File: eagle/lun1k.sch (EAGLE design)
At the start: 102 parts, among them IC1 MCP1700, IC2 LM27313, IC3 STM32F405RGT, IC4 NRF24L01SMD, IC5 MCP73833, J2 XF2-3015-1LW, Q1 Q12M-SMD-S, Q2 3.2X2.5CRYSTAL, SW1 JS102011SAQN, T1 SI2301DS, T5 SI2301DS, T6 SI2301DS, U1 N35P112, X1 MICROUSB, X1_ JST-PH3

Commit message: placed buttons
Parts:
- added SW2, SW3, SW4: SWITCH_MCTAEF, seb:SWITCH_MCTAEF
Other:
- note added: "BUTTONS"
- note added: "JOYSTICK"
- note removed: "NAVIGATION BUTTON"
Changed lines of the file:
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@@
 <layer number="110" name="fp0" color="7" fill="1" visible="no" active="yes"/>
 <layer number="111" name="LPC17xx" color="7" fill="1" visible="yes" active="yes"/>
+<layer number="112" name="tSilk" color="7" fill="1" visible="yes" active="yes"/>
 <layer number="116" name="Patch_BOT" color="9" fill="4" visible="yes" active="yes"/>
 <layer number="121" name="_tsilk" color="7" fill="1" visible="yes" active="yes"/>
@@
 <layer number="124" name="bTestmark" color="7" fill="1" visible="no" active="yes"/>
 <layer number="125" name="_tNames" color="7" fill="1" visible="yes" active="yes"/>
+<layer number="126" name="_bNames" color="7" fill="1" visible="yes" active="yes"/>
+<layer number="127" name="_tValues" color="7" fill="1" visible="yes" active="yes"/>
+<layer number="128" name="_bValues" color="7" fill="1" visible="yes" active="yes"/>
 <layer number="131" name="tAdjust" color="7" fill="1" visible="no" active="yes"/>
 <layer number="132" name="bAdjust" color="7" fill="1" visible="no" active="yes"/>
 <layer number="144" name="Drill_legend" color="7" fill="1" visible="yes" active="yes"/>
 <layer number="151" name="HeatSink" color="7" fill="1" visible="yes" active="yes"/>
+<layer number="152" name="_bDocu" color="7" fill="1" visible="yes" active="yes"/>
 <layer number="199" name="Contour" color="7" fill="1" visible="yes" active="yes"/>
 <layer number="200" name="200bmp" color="1" fill="10" visible="yes" active="yes"/>
@@
 <layer number="223" name="223bmp" color="24" fill="1" visible="no" active="no"/>
 <layer number="224" name="224bmp" color="25" fill="1" visible="no" active="no"/>
+<layer number="248" name="Housing" color="7" fill="1" visible="yes" active="yes"/>
+<layer number="249" name="Edge" color="7" fill="1" visible="yes" active="yes"/>
 <layer number="250" name="Descript" color="3" fill="1" visible="no" active="no"/>
 <layer number="251" name="SMDround" color="12" fill="11" visible="no" active="no"/>
@@
 <part name="R28" library="SparkFun" deviceset="RESISTOR" device="0402-RES" value="10k"/>
 <part name="R29" library="SparkFun" deviceset="RESISTOR" device="0402-RES" value="10k"/>
+<part name="SW2" library="seb" deviceset="SWITCH_MCTAEF" device=""/>
+<part name="SW3" library="seb" deviceset="SWITCH_MCTAEF" device=""/>
+<part name="SW4" library="seb" deviceset="SWITCH_MCTAEF" device=""/>
 </parts>
 <sheets>
@@
 <text x="137.16" y="157.48" size="2.54" layer="94">LEDs</text>
 <text x="193.04" y="157.48" size="2.54" layer="94">(optional) SD CARD</text>
-<text x="345.44" y="157.48" size="2.54" layer="94">NAVIGATION BUTTON</text>
+<text x="345.44" y="157.48" size="2.54" layer="94">JOYSTICK</text>
 <text x="2.54" y="99.06" size="2.54" layer="94">CPU</text>
 <text x="180.34" y="114.3" size="2.54" layer="94">RADIO</text>
@@
 <text x="431.8" y="132.08" size="1.778" layer="91">Leave SJ1 open for I2C Addr 0x41</text>
 <text x="431.8" y="129.54" size="1.778" layer="91">Close SJ1 for I2C Addr 0x40</text>
+<text x="139.7" y="203.2" size="2.54" layer="94">BUTTONS</text>
 </plain>
 <instances>
@@
 <instance part="R28" gate="G$1" x="485.14" y="167.64" rot="R90"/>
 <instance part="R29" gate="G$1" x="495.3" y="167.64" rot="R90"/>
+<instance part="SW2" gate="G$1" x="157.48" y="172.72" smashed="yes" rot="MR0">
+<attribute name="NAME" x="149.225" y="168.91" size="1.778" layer="95" rot="MR0"/>
+</instance>
+<instance part="SW3" gate="G$1" x="157.48" y="180.34" smashed="yes" rot="MR0">
+<attribute name="NAME" x="149.225" y="176.53" size="1.778" layer="95" rot="MR0"/>
+</instance>
+<instance part="SW4" gate="G$1" x="157.48" y="187.96" smashed="yes" rot="MR0">
+<attribute name="NAME" x="149.225" y="184.15" size="1.778" layer="95" rot="MR0"/>
+</instance>
 </instances>
 <busses>

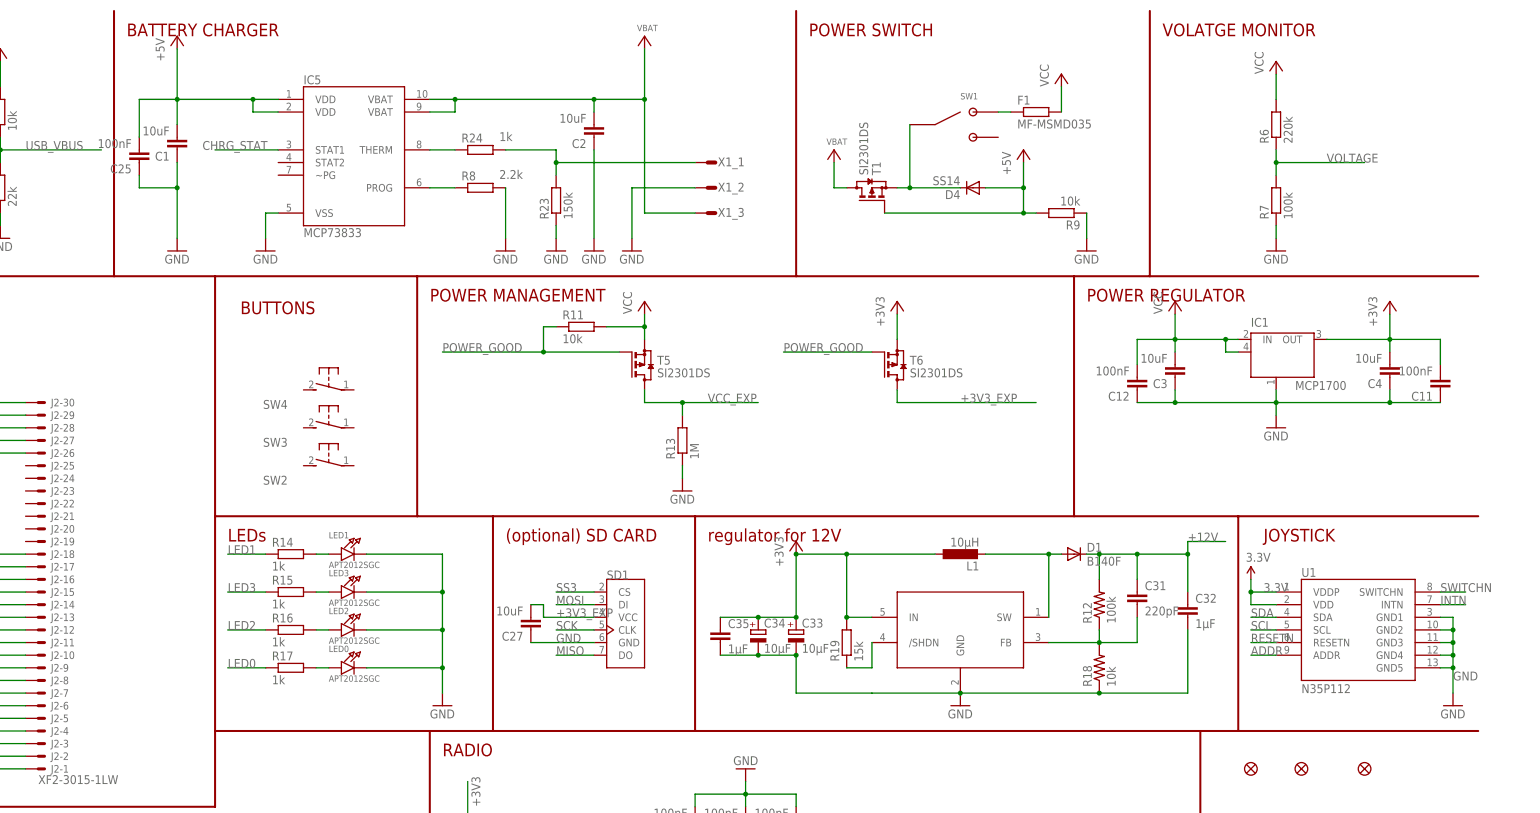
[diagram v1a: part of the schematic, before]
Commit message: completely removed old supply & management
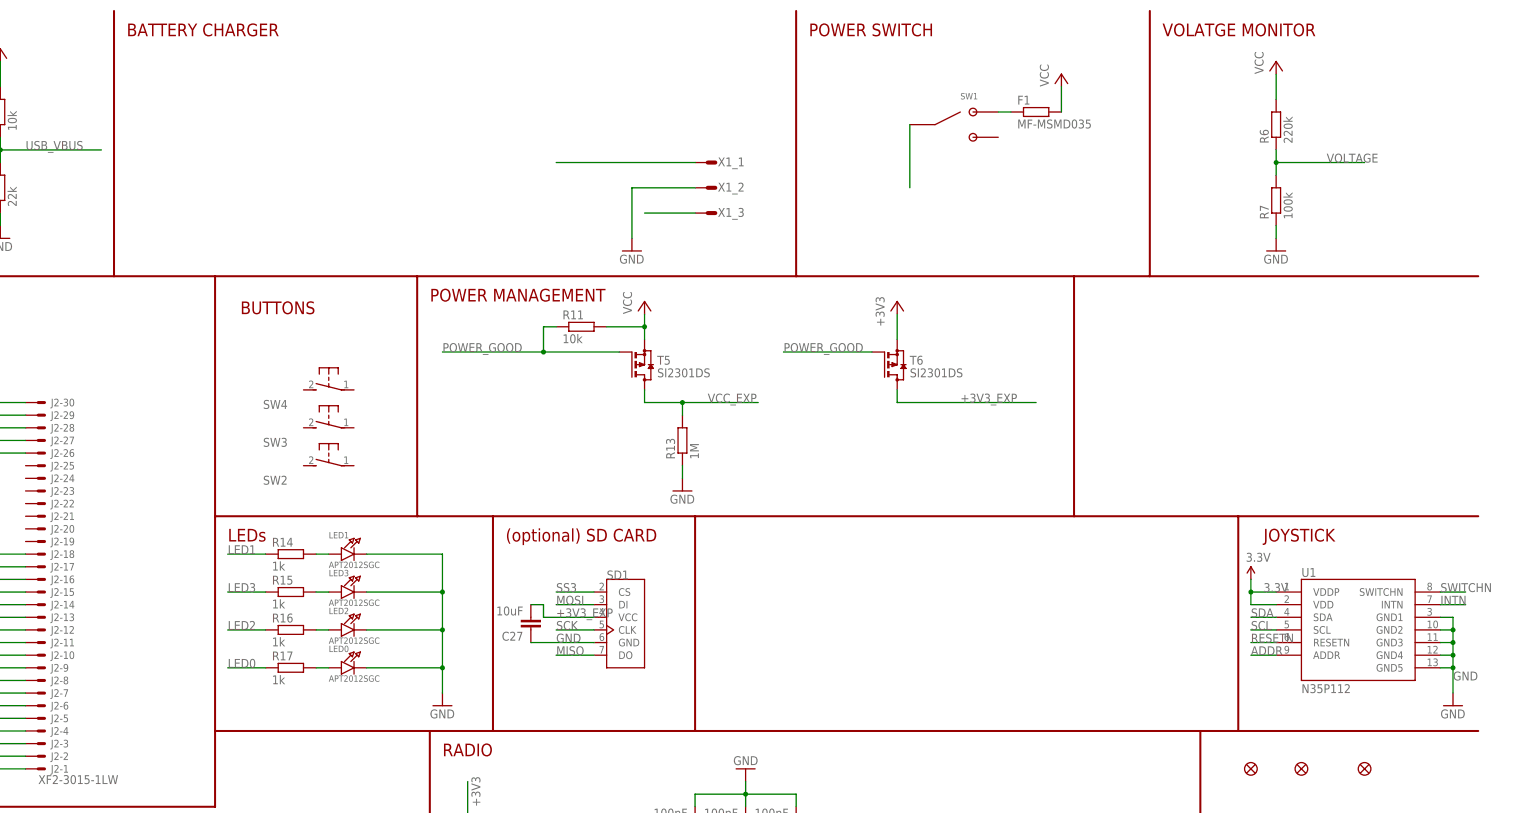
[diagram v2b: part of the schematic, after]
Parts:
- removed C1, C2, C3, C4: 10uF, rcl:C-EUC0805K
- removed C11, C12, C25: 100nF, SparkFun-Capacitors:CAP0402-CAP
- removed C31: 220pF, SparkFun:CAP0805
- removed C32, C35: 1µF, SparkFun:CAP0805
- removed C33, C34: 10µF, rcl:CPOL-EUSMCA
- removed D1: B140F, diode:DIODE-DO214AC
- removed D4: SS14, diode:DIODE-SMB
- removed IC1: MCP1700, badge:MCP1700
- removed IC2: LM27313, seb:LM27313
- removed IC5: MCP73833, SparkFun:MCP73833
- removed L1: 10µH, resistor:L-EUL1812
- removed R12: 100k, SparkFun:RESISTOR0805-RES
- removed R18: 10k, SparkFun:RESISTOR0805-RES
- removed R19: 15k, rcl:R-EU_R0402
- removed R23: 150k, rcl:R-EU_R0603
- removed R24: 1k, rcl:R-EU_R0603
- removed R8: 2.2k, rcl:R-EU_R0603
- removed R9: 10k, rcl:R-EU_R0603
- removed T1: SI2301DS, transistor-small-signal:BSS84
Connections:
- removed net CHRG_STAT: IC5.STAT1
- removed net N$13: IC5.PROG, R8.2
- removed net N$16: D1.A, IC2.SW, L1.2
- removed net N$17: C31.2, IC2.FB, R12.1, R18.2
- removed net N$18: IC2./SHDN, R19.1
- removed net N$2: IC5.THERM, R24.2
- removed net N$7: R23.2, R24.1, X1_1.1
- removed net VBAT: C2.2, IC5.VBAT@1, IC5.VBAT@2, T1.D, X1_3.1
- new net N$21: X1_3.1
- new net VLIPO: X1_1.1
- net +12V: no longer C31.1, C32.1, D1.C, R12.2
- net +3V3: no longer C11.2, C33.+, C34.+, C35.1, C4.2, IC1.OUT, IC2.IN, L1.1, R19.2
- net +5V: no longer C1.2, C25.2, D4.A, IC5.VDD@1, IC5.VDD@2, R9.2, T1.G
- net GND: no longer C1.1, C11.1, C12.1, C2.1, C25.1, C3.1, C32.2, C33.-, C34.-, C35.2, C4.1, IC1.GND/ADJ, IC2.GND, IC5.VSS, R18.1, R23.1, R8.1, R9.1
- net N$8: no longer D4.C, T1.S
- net VCC: no longer C12.2, C3.2, IC1.IN, IC1.IN@1
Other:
- note removed: "POWER REGULATOR"
- note removed: "regulator for 12V"

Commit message: some resistors: 0603 -> 0402
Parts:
- R11, R13, R2, R3, R4, R5, R6, R7: device rcl:R-EU_R0603 -> SparkFun-Passives:RESISTOR0402-RES
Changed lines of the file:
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@@
 <part name="P+5" library="supply1" deviceset="+5V" device=""/>
 <part name="GND9" library="supply1" deviceset="GND" device=""/>
-<part name="R4" library="rcl" deviceset="R-EU_" device="R0603" value="10k"/>
-<part name="R5" library="rcl" deviceset="R-EU_" device="R0603" value="22k"/>
+<part name="R4" library="SparkFun-Passives" deviceset="RESISTOR" device="0402-RES" value="10k"/>
+<part name="R5" library="SparkFun-Passives" deviceset="RESISTOR" device="0402-RES" value="22k"/>
 <part name="GND10" library="supply1" deviceset="GND" device=""/>
 <part name="P+6" library="supply1" deviceset="+5V" device=""/>
-<part name="R2" library="rcl" deviceset="R-EU_" device="R0603" value="33"/>
-<part name="R3" library="rcl" deviceset="R-EU_" device="R0603" value="33"/>
+<part name="R2" library="SparkFun-Passives" deviceset="RESISTOR" device="0402-RES" value="33"/>
+<part name="R3" library="SparkFun-Passives" deviceset="RESISTOR" device="0402-RES" value="33"/>
 <part name="GND11" library="supply1" deviceset="GND" device=""/>
 <part name="Q1" library="seb" deviceset="X22-OSCILLATOR" device="" value="Q12M-SMD-S"/>
@@
 <part name="+3V6" library="supply1" deviceset="+3V3" device=""/>
 <part name="P+10" library="supply1" deviceset="VCC" device=""/>
-<part name="R11" library="rcl" deviceset="R-EU_" device="R0603" value="10k"/>
-<part name="R6" library="rcl" deviceset="R-EU_" device="R0603" value="220k"/>
-<part name="R7" library="rcl" deviceset="R-EU_" device="R0603" value="100k"/>
+<part name="R11" library="SparkFun-Passives" deviceset="RESISTOR" device="0402-RES" value="10k"/>
+<part name="R6" library="SparkFun-Passives" deviceset="RESISTOR" device="0402-RES" value="220k"/>
+<part name="R7" library="SparkFun-Passives" deviceset="RESISTOR" device="0402-RES" value="100k"/>
 <part name="GND18" library="supply1" deviceset="GND" device=""/>
 <part name="P+7" library="supply1" deviceset="VCC" device=""/>
@@
 <part name="GND28" library="supply1" deviceset="GND" device=""/>
 <part name="R22" library="rcl" deviceset="R-EU_" device="R0603" value="R1002-1%63"/>
-<part name="R13" library="rcl" deviceset="R-EU_" device="R0603" value="1M"/>
+<part name="R13" library="SparkFun-Passives" deviceset="RESISTOR" device="0402-RES" value="1M"/>
 <part name="GND1" library="supply1" deviceset="GND" device=""/>
 <part name="X1_" library="badge" deviceset="JST-PH3" device=""/>

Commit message: some resistors: 0603 -> 0402
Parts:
- R14, R15, R16, R17: device rcl:R-EU_R0603 -> SparkFun-Passives:RESISTOR0402-RES
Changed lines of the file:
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@@
 <part name="LED2" library="microbuilder" deviceset="LED" device="0805" value="APT2012SGC"/>
 <part name="LED0" library="microbuilder" deviceset="LED" device="0805" value="APT2012SGC"/>
-<part name="R14" library="rcl" deviceset="R-EU_" device="R0603" value="1k"/>
+<part name="R14" library="SparkFun-Passives" deviceset="RESISTOR" device="0402-RES" value="1k"/>
 <part name="C9" library="SparkFun-Capacitors" deviceset="CAP" device="0402-CAP" value="22pF"/>
 <part name="P+5" library="supply1" deviceset="+5V" device=""/>
@@
 <part name="C10" library="SparkFun-Capacitors" deviceset="CAP" device="0402-CAP" value="22pF"/>
 <part name="GND13" library="supply1" deviceset="GND" device=""/>
-<part name="R15" library="rcl" deviceset="R-EU_" device="R0603" value="1k"/>
-<part name="R16" library="rcl" deviceset="R-EU_" device="R0603" value="1k"/>
-<part name="R17" library="rcl" deviceset="R-EU_" device="R0603" value="1k"/>
+<part name="R15" library="SparkFun-Passives" deviceset="RESISTOR" device="0402-RES" value="1k"/>
+<part name="R16" library="SparkFun-Passives" deviceset="RESISTOR" device="0402-RES" value="1k"/>
+<part name="R17" library="SparkFun-Passives" deviceset="RESISTOR" device="0402-RES" value="1k"/>
 <part name="+3V6" library="supply1" deviceset="+3V3" device=""/>
 <part name="P+10" library="supply1" deviceset="VCC" device=""/>

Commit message: new lipo charger
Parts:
- added C1, C12: 10µF, SparkFun:CAP0805
- added C11, C7: 10pF, SparkFun:CAP0805
- added C2: 22µF, SparkFun:CAP0805
- added C3: 33pF, SparkFun:CAP0805
- added C4: 330pF, SparkFun:CAP0805
- added C8: 1µF, SparkFun:CAP0805
- added IC1: LTC3558, seb:LTC3558
- added L1: 2,2µH, seb:SMD-INDUCTOR-4012
- added L5: 4,7µF, seb:VLF4012A
- added R12: 15k, SparkFun-Resistors:RESISTOR0805-RES
- added R18: 121k, SparkFun-Resistors:RESISTOR0805-RES
- added R19: 1k, SparkFun-Resistors:RESISTOR0805-RES
- added R24, R30, R31: 680k, SparkFun-Resistors:RESISTOR0402-RES
- added R32: 470k, SparkFun-Resistors:RESISTOR0805-RES
- added R33: 150k, SparkFun-Resistors:RESISTOR0805-RES
- added R8: 130k, SparkFun-Resistors:RESISTOR0805-RES
- added R9: 680k, SparkFun-Resistors:RESISTOR0805-RES
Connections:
- removed net N$15: F1.1, SW1.1
- removed net N$8: SW1.2
- new net EN2: IC1.EN2, IC3.PB12, R24.2
- new net N$13: C3.2, R18.1
- new net N$16: C4.2, R12.1
- new net N$17: C4.1, C7.1, IC1.VC2
- new net N$18: IC1.SWCD2, L1.P$1
- new net N$2: IC1.PROG, R19.2
- new net N$22: IC1.SWAB2, L1.P$2
- new net N$23: IC1.CHRG, IC3.PB13
- new net N$25: IC1.MODE, IC1.SUSP, R30.1
- new net N$27: IC1.EN1, R31.2, SW1.3
- new net N$28: C11.1, IC1.FB1, R32.1, R33.2
- new net N$29: IC1.SW1, L5.1
- new net N$7: C3.1, C7.2, IC1.FB2, R12.2, R8.2, R9.1
- net +12V: now also C2.2, IC1.VOUT2, R18.2, R9.2
- net +5V: now also C8.2, IC1.HPWR, IC1.VCC
- net 3.3V: now also C11.2, C12.2, L5.2, R32.2
- net GND: now also C1.2, C12.1, C2.1, C8.1, IC1.GND, IC1.NTC, IC1.PAD, R19.1, R24.1, R30.2, R31.1, R33.1, R8.1
- net VLIPO: now also C1.1, IC1.BAT, IC1.PVIN1, IC1.PVIN2, SW1.2
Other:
- note added: "115k"
- note added: "120k"
- note added: "130k"
- note added: "3,3V"
- note added: "360k"
- note added: "4,98V"
- note added: "5V"
- note added: "630k"
- note added: "680k"
- note added: "R1"
- note added: "R2"
- moved on the sheet: SW1

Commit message: routing
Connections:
- net +3V3: now also C11.2, C12.2, L5.2, R32.2, U1.VDD, U1.VDDP
- net 3.3V: no longer C11.2, C12.2, L5.2, R32.2, U1.VDD, U1.VDDP
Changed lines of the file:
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@@
 <pinref part="+3V10" gate="G$1" pin="+3V3"/>
+</segment>
+<segment>
+<wire x1="584.2" y1="71.12" x2="594.36" y2="71.12" width="0.1524" layer="91"/>
+<wire x1="594.36" y1="71.12" x2="604.52" y2="71.12" width="0.1524" layer="91"/>
+<wire x1="604.52" y1="71.12" x2="604.52" y2="76.2" width="0.1524" layer="91"/>
+<wire x1="574.04" y1="71.12" x2="584.2" y2="71.12" width="0.1524" layer="91"/>
+<junction x="584.2" y="71.12"/>
+<junction x="594.36" y="71.12"/>
+<junction x="604.52" y="71.12"/>
+<pinref part="R32" gate="G$1" pin="2"/>
+<pinref part="C11" gate="G$1" pin="2"/>
+<pinref part="C12" gate="G$1" pin="2"/>
+<pinref part="L5" gate="G$1" pin="2"/>
+<pinref part="P+4" gate="G$1" pin="3.3V"/>
+</segment>
+<segment>
+<wire x1="342.9" y1="149.86" x2="342.9" y2="147.32" width="0.1524" layer="91"/>
+<wire x1="342.9" y1="147.32" x2="347.98" y2="147.32" width="0.1524" layer="91"/>
+<wire x1="347.98" y1="144.78" x2="342.9" y2="144.78" width="0.1524" layer="91"/>
+<wire x1="342.9" y1="144.78" x2="342.9" y2="147.32" width="0.1524" layer="91"/>
+<junction x="342.9" y="147.32"/>
+<label x="345.44" y="147.32" size="1.778" layer="95"/>
+<pinref part="P+8" gate="G$1" pin="3.3V"/>
+<pinref part="U1" gate="G$1" pin="VDDP"/>
+<pinref part="U1" gate="G$1" pin="VDD"/>
 </segment>
 </net>
@@
 <net name="3.3V" class="0">
 <segment>
-<wire x1="342.9" y1="149.86" x2="342.9" y2="147.32" width="0.1524" layer="91"/>
-<wire x1="342.9" y1="147.32" x2="347.98" y2="147.32" width="0.1524" layer="91"/>
-<wire x1="347.98" y1="144.78" x2="342.9" y2="144.78" width="0.1524" layer="91"/>
-<wire x1="342.9" y1="144.78" x2="342.9" y2="147.32" width="0.1524" layer="91"/>
-<junction x="342.9" y="147.32"/>
-<label x="345.44" y="147.32" size="1.778" layer="95"/>
-<pinref part="P+8" gate="G$1" pin="3.3V"/>
-<pinref part="U1" gate="G$1" pin="VDDP"/>
-<pinref part="U1" gate="G$1" pin="VDD"/>
-</segment>
-<segment>
 <wire x1="444.5" y1="177.8" x2="444.5" y2="175.26" width="0.1524" layer="91"/>
 <wire x1="444.5" y1="175.26" x2="444.5" y2="172.72" width="0.1524" layer="91"/>
@@
 <label x="426.72" y="116.84" size="1.778" layer="95" font="vector"/>
 </segment>
-<segment>
-<wire x1="584.2" y1="71.12" x2="594.36" y2="71.12" width="0.1524" layer="91"/>
-<wire x1="594.36" y1="71.12" x2="604.52" y2="71.12" width="0.1524" layer="91"/>
-<wire x1="604.52" y1="71.12" x2="604.52" y2="76.2" width="0.1524" layer="91"/>
-<wire x1="574.04" y1="71.12" x2="584.2" y2="71.12" width="0.1524" layer="91"/>
-<junction x="584.2" y="71.12"/>
-<junction x="594.36" y="71.12"/>
-<junction x="604.52" y="71.12"/>
-<pinref part="R32" gate="G$1" pin="2"/>
-<pinref part="C11" gate="G$1" pin="2"/>
-<pinref part="C12" gate="G$1" pin="2"/>
-<pinref part="L5" gate="G$1" pin="2"/>
-<pinref part="P+4" gate="G$1" pin="3.3V"/>
-</segment>
-</net>
+</net>
